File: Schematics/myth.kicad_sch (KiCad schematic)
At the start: 135 parts, among them J1 Conn_01x08_Male, J10 Conn_01x04_Male, J11 Conn_02x01, J2 Conn_01x08_Male, J3 Conn_01x08_Male, J4 Conn_01x08_Male, J5 Conn_01x08_Male, J6 Conn_01x08_Male, J8 Conn_01x08_Male, J9 Conn_01x04_Male, U1 74AHC02, U10 74HC595, U11 74HC165, U12 74AHC08, U13 74HC238, U14 74HC238, U15 74HC238, U16 4002, U17 74HC32, U18 74AHC273, U19 74LS32, U2 74AHC273, U20 CD4532BE, U21 74AHC138, U22 74AHC04, U23 74AHC138, U24 74HC238, U25 74HC238, U26 74LS32, U27 4078, U28 74AHC244, U29 74AHC138, U3 74HC74, U30 74AHC138, U31 4075, U32 74AHC02, U33 74AHC138, U34 74HC238, U35 74AHC138, U36 74HC163, U37 74AHC574, U38 74HC238, U39 74HC32, U4 74AHC04, U40 74AHC04, U41 74AHC574, U42 74HC74, U43 74AHC273, U44 74HC283, U45 74HC283, U46 74AHC273, U47 74HC02, U48 74HC157, U49 74HC157, U5 74AHC04, U50 74AHC244, U51 74AHC04, U52 74AHC574, U53 74HC193, U54 74HC193, U55 74HC193, U56 74HC193, U57 74HC193, U58 74HC193, U59 74HC193, U6 74AHC08, U60 74AHC244, U61 74LS32, U62 4078, U63 74AHC244, U64 74LS21, U65 74AHC04, U66 74AHC273, U67 74HC157, U68 74HC157, U69 74HC157, U7 74HC00, U70 74HC157, U71 74LS257, U72 74LS257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

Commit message: Change GETPUT opcode encoding
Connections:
- net IB0: now also U75.2 (1A0); no longer U9.1 (A0)
- net IB1: now also U75.4 (1A1); no longer U9.2 (A1)
- net IB2: now also U75.6 (1A2); no longer U9.3 (A2)
- net IB3: now also U9.3 (A2); no longer U75.2 (1A0)
- net IB4: now also U9.1 (A0); no longer U75.4 (1A1)
- net IB5: now also U9.2 (A1); no longer U75.6 (1A2)
- net PAR_CP renamed SH1_PARCP
- net ~{PAR_OE} renamed ~{SL1_PAROE}
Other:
- note added: "IB 0-2 are the immediate offset for GET-PUT operations"
- note added: "IB0-2 is byte offset"
- note added: "Instruction byte: all0: OPC_SYS 00000 xxx See table @ SYS decoder else: OPC_ADJUST 00001 xxx b2:extended sign bit b1-0 LSB OPC_ALU 0001x xxx See table @ ALU OPC_TRAP 001xx xxx b4:MSB b3-0:LSB (remaining bits set 1) OPC_GETPUT 01xxx xxx b0-2 OFFS b3:GP B4-5:REG(RODG) OPC_PAIR 1xxxx xxx DEST SRC"
- note added: "NML => INO NMD => DEO MLML => NOP (reserved) MLML => NOP (reserved) MDML => NOP (reserved) MDMD => NOP (reserved) GG => NOP (reserved) RR => NOP (reserved) II => NOP (reserved)"
- note added: "Remap ("scrounge") GG, RR, II etc, and impracticable opcodes such as N-MD"
- note added: "SH0_NULL device"
- note added: "~{SL0_NULL} device"
- note removed: "IB 3-5 are the immediate offset for GET-PUT operations"
- note removed: "IB3-5 is byte offset"
- note removed: "Instruction byte: all0: OPC_SYS 00000 xxx See table @ SYS decoder else: OPC_ADJUST 00001 xxx b2:extended sign bit b1-0 LSB OPC_ALU 0001x xxx See table @ ALU OPC_TRAP 001xx xxx b4:MSB b3-0:LSB (remaining bits set 1) OPC_GETPUT 01xxx xxx b5-3 OFFS b2:GL b1:GP B0:RO OPC_PAIR 1xxxx xxx DEST SRC"
- note removed: "NULL device"
- note removed: "Remap ("scrounge") RR, II etc, and impracticable opcodes such as N-MD"
- moved on the sheet: U18, U24, U25, U29, U30

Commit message: Update schematics file
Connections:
- net MDx renamed Mx
- net MDx_pre renamed Mx_pre
- net MLx renamed Lx
- net MLx_pre renamed Lx_pre
- net xGI renamed xA
- net xJF renamed xF
- net xJT renamed xT
- net xJW renamed xW
- net xJW_pre renamed xW_pre
- net xMD_pre renamed xM_pre
- net xML_pre renamed xL_pre
- net ~{MDx} renamed ~{Mx}
- net ~{MLx} renamed ~{Lx}
- net ~{xJW} renamed ~{xW}
- net ~{xMD} renamed ~{xM}
- net ~{xML} renamed ~{xL}
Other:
- note added: "NL => INO NM => DEO LL => NOP (reserved) LM => NOP (reserved) ML => NOP (reserved) MM => NOP (reserved) GG => NOP (reserved) RR => NOP (reserved) II => NOP (reserved)"
- note added: "Remap ("scrounge") GG, RR, II etc, and impracticable opcodes such as NM"
- note added: "To do: Fix logic above to map NL to INO, and NM to DEO"
- note removed: "NML => INO NMD => DEO MLML => NOP (reserved) MLML => NOP (reserved) MDML => NOP (reserved) MDMD => NOP (reserved) GG => NOP (reserved) RR => NOP (reserved) II => NOP (reserved)"
- note removed: "Remap ("scrounge") GG, RR, II etc, and impracticable opcodes such as N-MD"
- note removed: "To do: Fix logic above to map NML to INO, and NMD to DEO"
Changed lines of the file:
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@@
 		)
 	)
-	(text "                   NML  => INO\n                   NMD  => DEO\n                   MLML => NOP (reserved)\n                   MLML => NOP (reserved)\n                   MDML => NOP (reserved)\n                   MDMD => NOP (reserved)\n                   GG   => NOP (reserved)\n                   RR   => NOP (reserved)\n                   II   => NOP (reserved)"
+	(text "                   NL => INO\n                   NM => DEO\n                   LL => NOP (reserved)\n                   LM => NOP (reserved)\n                   ML => NOP (reserved)\n                   MM => NOP (reserved)\n                   GG => NOP (reserved)\n                   RR => NOP (reserved)\n                   II => NOP (reserved)"
 		(exclude_from_sim no)
 		(at 188.028 312.557 0)
@@
 		)
 	)
-	(text "To do:\nFix logic above\nto map NML to INO,\nand NMD to DEO"
+	(text "To do:\nFix logic above\nto map NL to INO,\nand NM to DEO"
 		(exclude_from_sim no)
 		(at 190.62 300.8412 0)
@@
 		)
 	)
-	(text "Remap (\"scrounge\") GG, RR, II etc,\nand impracticable opcodes such as N-MD"
+	(text "Remap (\"scrounge\") GG, RR, II etc,\nand impracticable opcodes such as NM"
 		(exclude_from_sim no)
 		(at 219.7394 228.2457 0)
@@
 		)
 	)
-	(label "~{MDx}"
+	(label "~{Mx}"
 		(at 705.7307 273.4183 180)
 		(fields_autoplaced yes)
@@
 		)
 	)
-	(label "~{xMD}"
+	(label "~{xM}"
 		(at 1123.5198 503.8164 0)
 		(fields_autoplaced yes)
@@
 		)
 	)
-	(label "xJT"
+	(label "xT"
 		(at 63.9318 196.3674 180)
 		(fields_autoplaced yes)
@@
 		)
 	)
-	(label "xJW"
+	(label "xW"
 		(at 745.0077 134.3281 180)
 		(fields_autoplaced yes)
@@
 		)
 	)
-	(label "xGI"
+	(label "xA"
 		(at 364.9218 304.4698 0)
 		(fields_autoplaced yes)
@@
 		)
 	)
-	(label "xJW_pre"
+	(label "xW_pre"
 		(at 63.9318 191.2874 180)
 		(fields_autoplaced yes)
@@
 		)
 	)
-	(label "~{xML}"
+	(label "~{xL}"
 		(at 364.2868 268.9098 0)
 		(fields_autoplaced yes)
@@
 		)
 	)
-	(label "MDx_pre"
+	(label "Mx_pre"
 		(at 137.3886 380.1872 0)
 		(fields_autoplaced yes)
@@
 		)
 	)
-	(label "MLx"
+	(label "Lx"
 		(at 759.5384 199.9363 0)
 		(fields_autoplaced yes)
@@
 		)
 	)
-	(label "~{xML}"
+	(label "~{xL}"
 		(at 1123.5198 506.3564 0)
 		(fields_autoplaced yes)
@@
 		)
 	)
-	(label "xMD_pre"
+	(label "xM_pre"
 		(at 957.9938 695.1442 180)
 		(fields_autoplaced yes)
@@
 		)
 	)
-	(label "MLx_pre"
+	(label "Lx_pre"
 		(at 137.3886 382.7272 0)
 		(fields_autoplaced yes)
@@
 		)
 	)
-	(label "MDx_pre"
+	(label "Mx_pre"
 		(at 957.9938 690.0642 180)
 		(fields_autoplaced yes)
@@
 		)
 	)
-	(label "xGI"
+	(label "xA"
 		(at 594.1685 186.1343 180)
 		(fields_autoplaced yes)
@@
 		)
 	)
-	(label "~{xJW}"
+	(label "~{xW}"
 		(at 760.2477 134.3281 0)
 		(fields_autoplaced yes)
@@
 		)
 	)
-	(label "MLx_pre"
+	(label "Lx_pre"
 		(at 703.1814 523.1929 180)
 		(fields_autoplaced yes)
@@
 		)
 	)
-	(label "xGI"
+	(label "xA"
 		(at 562.7742 167.7322 180)
 		(fields_autoplaced yes)
@@
 		)
 	)
-	(label "xJW_pre"
+	(label "xW_pre"
 		(at 131.6482 269.5702 0)
 		(fields_autoplaced yes)
@@
 		)
 	)
-	(label "xJT"
+	(label "xT"
 		(at 364.9218 314.6298 0)
 		(fields_autoplaced yes)
@@
 		)
 	)
-	(label "MDx"
+	(label "Mx"
 		(at 720.9707 273.4183 0)
 		(fields_autoplaced yes)
@@
 		)
 	)
-	(label "xML_pre"
+	(label "xL_pre"
 		(at 175.1584 279.1714 180)
 		(fields_autoplaced yes)
@@
 		)
 	)
-	(label "~{MDx}"
+	(label "~{Mx}"
 		(at 362.3818 376.2248 0)
 		(fields_autoplaced yes)
@@
 		)
 	)
-	(label "xJF"
+	(label "xF"
 		(at 364.9218 317.1698 0)
 		(fields_autoplaced yes)
@@
 		)
 	)
-	(label "~{xMD}"
+	(label "~{xM}"
 		(at 364.2868 266.3698 0)
 		(fields_autoplaced yes)
@@
 		)
 	)
-	(label "xML_pre"
+	(label "xL_pre"
 		(at 131.1148 316.5348 0)
 		(fields_autoplaced yes)
@@
 		)
 	)
-	(label "~{MLx}"
+	(label "~{Lx}"
 		(at 744.2984 199.9363 180)
 		(fields_autoplaced yes)
@@
 		)
 	)
-	(label "MLx"
+	(label "Lx"
 		(at 1109.2883 604.7814 0)
 		(fields_autoplaced yes)
@@
 		)
 	)
-	(label "xMD_pre"
+	(label "xM_pre"
 		(at 131.1148 313.9948 0)
 		(fields_autoplaced yes)
@@
 		)
 	)
-	(label "MDx_pre"
+	(label "Mx_pre"
 		(at 174.9866 261.5757 180)
 		(fields_autoplaced yes)
@@
 		)
 	)
-	(label "MDx"
+	(label "Mx"
 		(at 1109.2883 602.2414 0)
 		(fields_autoplaced yes)
@@
 		)
 	)
-	(label "~{xJW}"
+	(label "~{xW}"
 		(at 631.5591 667.5672 180)
 		(fields_autoplaced yes)
@@
 		)
 	)
-	(label "xMD_pre"
+	(label "xM_pre"
 		(at 175.1584 284.2514 180)
 		(fields_autoplaced yes)
@@
 		)
 	)
-	(label "xGI"
+	(label "xA"
 		(at 562.9238 225.3634 180)
 		(fields_autoplaced yes)
@@
 		)
 	)
-	(label "xJW"
+	(label "xW"
 		(at 364.9218 312.0898 0)
 		(fields_autoplaced yes)
@@
 		)
 	)
-	(label "xJF"
+	(label "xF"
 		(at 63.9318 198.9074 180)
 		(fields_autoplaced yes)
@@
 		)
 	)
-	(label "MLx_pre"
+	(label "Lx_pre"
 		(at 174.9866 256.4957 180)
 		(fields_autoplaced yes)
@@
 		)
 	)
-	(label "~{MLx}"
+	(label "~{Lx}"
 		(at 362.3818 378.7648 0)
 		(fields_autoplaced yes)
@@
 		)
 	)
-	(label "xML_pre"
+	(label "xL_pre"
 		(at 703.1814 528.2729 180)
 		(fields_autoplaced yes)

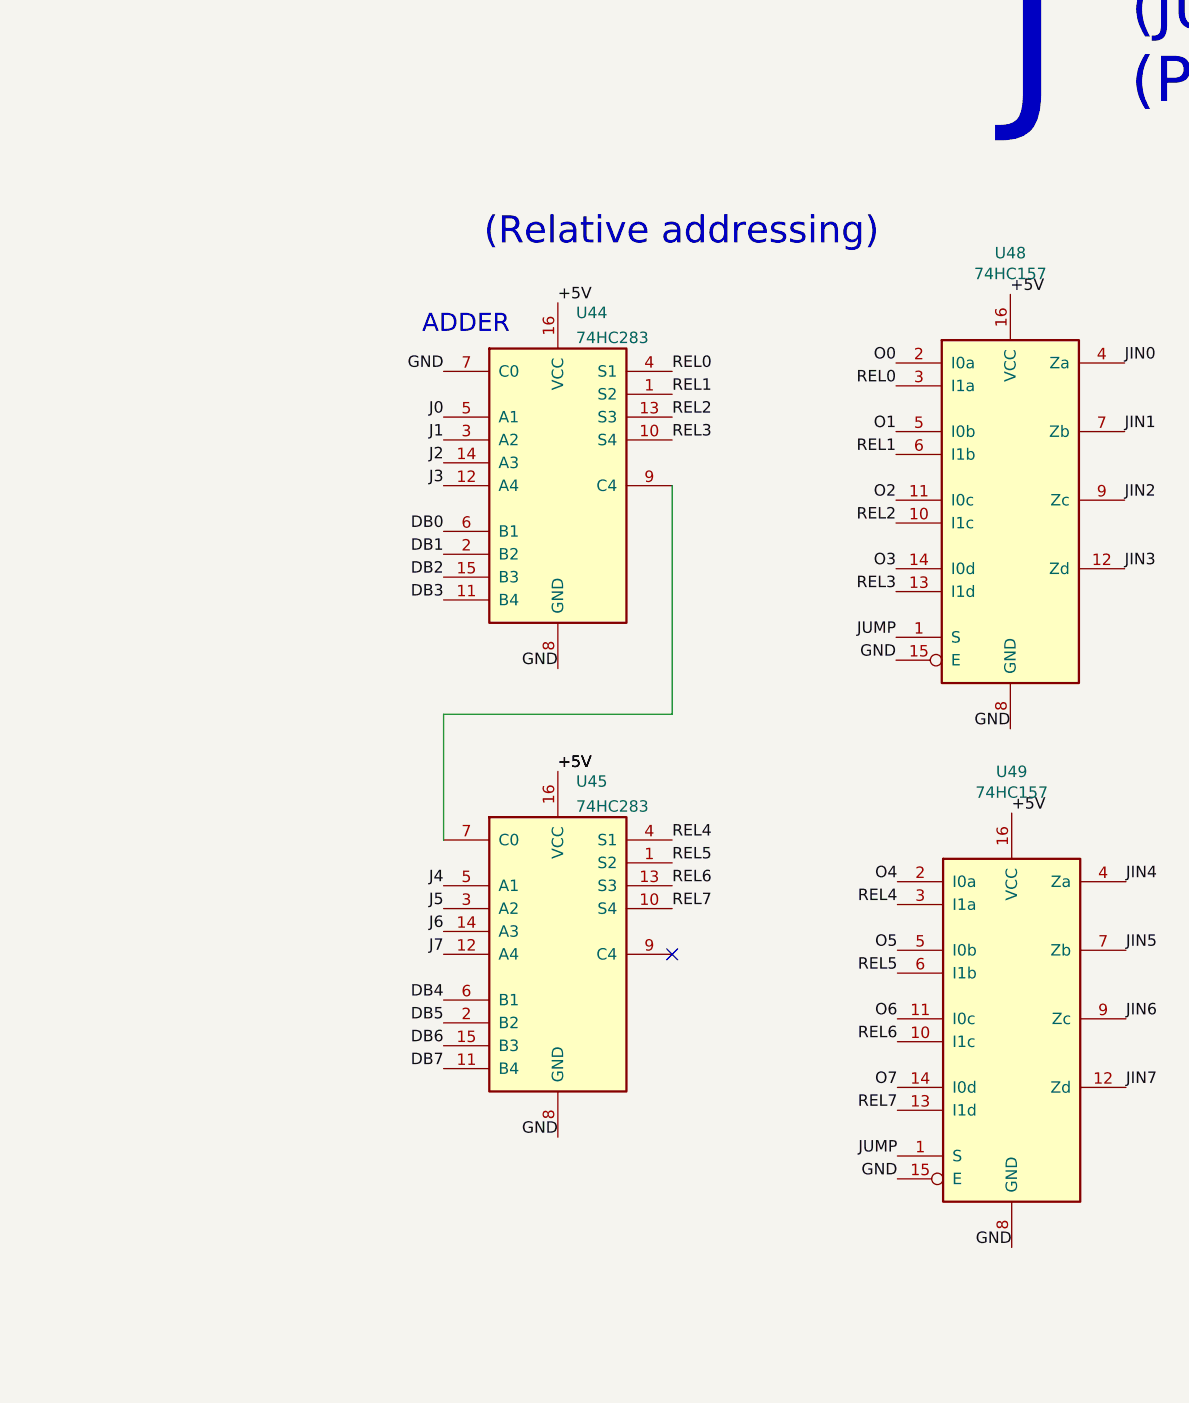
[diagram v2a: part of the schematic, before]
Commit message: Switch back to absolute addressing
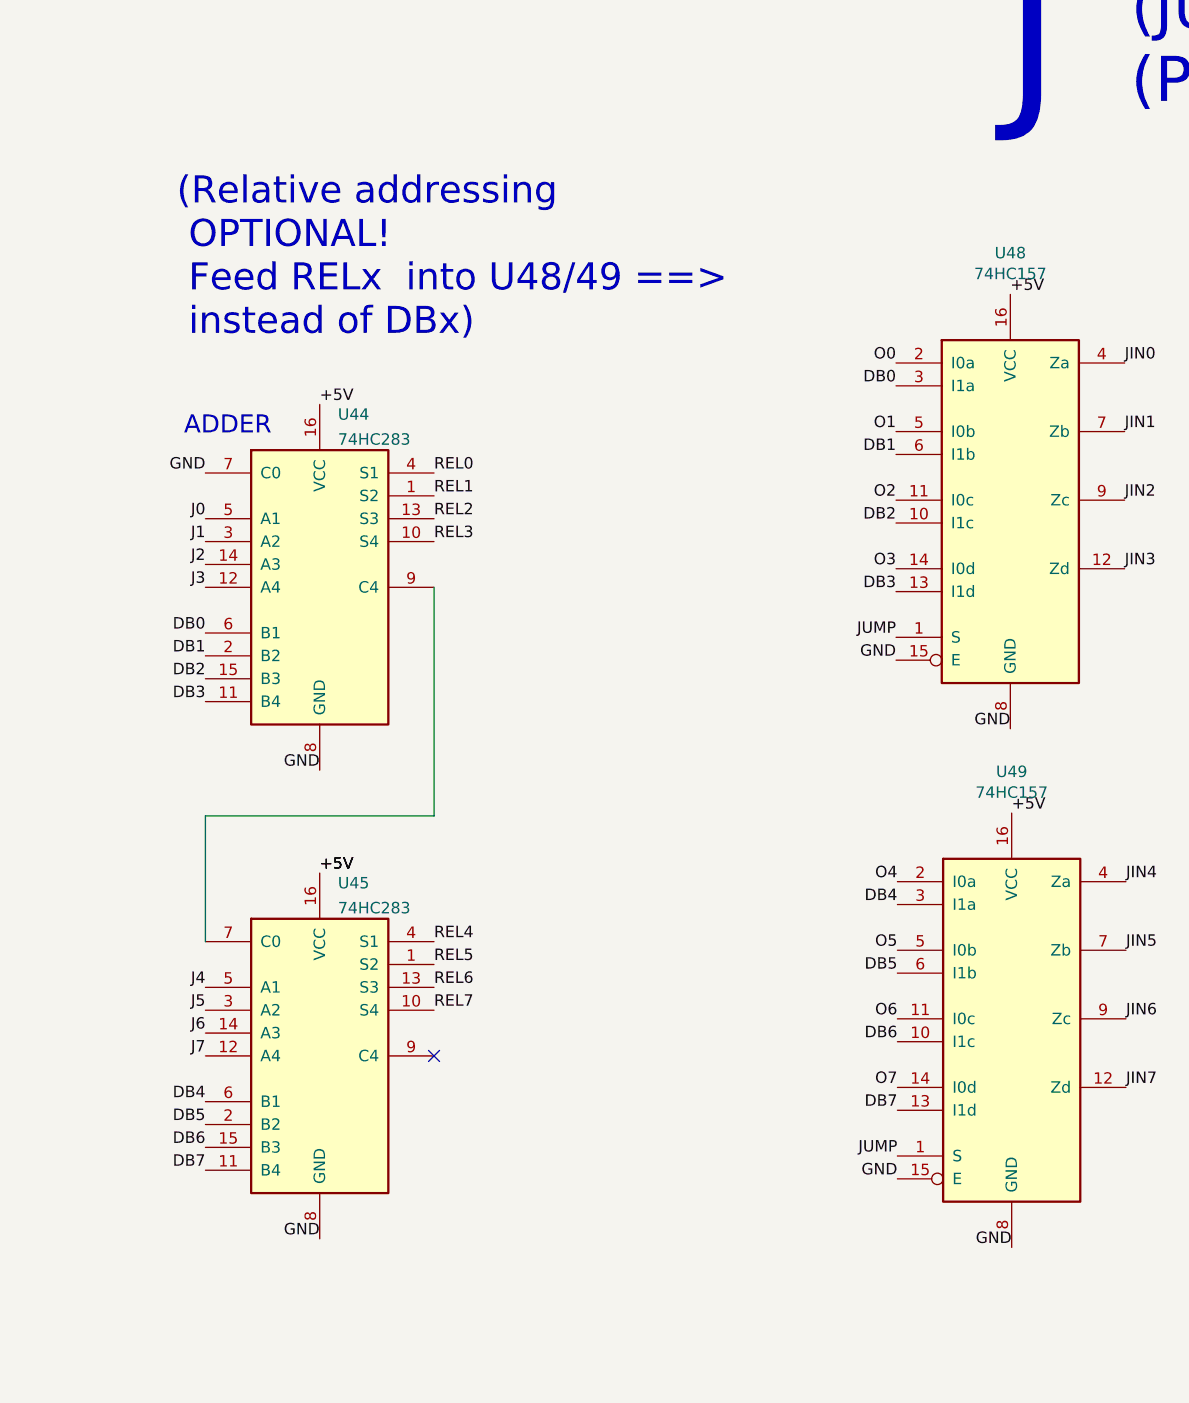
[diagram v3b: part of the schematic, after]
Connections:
- net DB0: now also U48.3 (I1a)
- net DB1: now also U48.6 (I1b)
- net DB2: now also U48.10 (I1c)
- net DB3: now also U48.13 (I1d)
- net DB4: now also U49.3 (I1a)
- net DB5: now also U49.6 (I1b)
- net DB6: now also U49.10 (I1c)
- net DB7: now also U49.13 (I1d)
- net REL0: no longer U48.3 (I1a)
- net REL1: no longer U48.6 (I1b)
- net REL2: no longer U48.10 (I1c)
- net REL3: no longer U48.13 (I1d)
- net REL4: no longer U49.3 (I1a)
- net REL5: no longer U49.6 (I1b)
- net REL6: no longer U49.10 (I1c)
- net REL7: no longer U49.13 (I1d)
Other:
- note added: "(Relative addressing OPTIONAL! Feed RELx into U48/49 ==> instead of DBx)"
- note removed: "(Relative addressing)"
- moved on the sheet: U44, U45
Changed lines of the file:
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@@
 	(title_block
 		(title "Sonne-8 Micro-Controller")
-		(date "2024-08-25")
+		(date "2024-08-26")
 		(rev "Myth")
 		(company "Contact: mim@ok-schalter.de")
@@
 	)
 	(no_connect
-		(at 472.4824 406.8887)
+		(at 446.0236 418.1813)
 	)
 	(no_connect
@@
 	(wire
 		(pts
-			(xy 447.0824 380.2187) (xy 447.0824 394.1887)
+			(xy 420.6236 391.5113) (xy 420.6236 405.4813)
 		)
 		(stroke
@@
 	(wire
 		(pts
-			(xy 472.4824 354.8187) (xy 472.4824 380.2187)
+			(xy 446.0236 366.1113) (xy 446.0236 391.5113)
 		)
 		(stroke
@@
 	(wire
 		(pts
-			(xy 472.4824 380.2187) (xy 447.0824 380.2187)
+			(xy 446.0236 391.5113) (xy 420.6236 391.5113)
 		)
 		(stroke
@@
 		)
 	)
-	(text "(Relative addressing)"
+	(text "(Relative addressing\n OPTIONAL!\n Feed RELx  into U48/49 ==>\n instead of DBx)\n"
 		(exclude_from_sim no)
-		(at 451.5615 328.3983 0)
+		(at 417.4367 338.4544 0)
 		(effects
 			(font
@@
 	(text "ADDER"
 		(exclude_from_sim no)
-		(at 444.6948 338.1055 0)
+		(at 418.236 349.3981 0)
 		(effects
 			(font
@@
 		)
 	)
-	(label "REL0"
+	(label "DB0"
 		(at 497.3579 343.7277 180)
 		(fields_autoplaced yes)
@@
 	)
 	(label "DB4"
-		(at 447.0824 411.9687 180)
+		(at 420.6236 423.2613 180)
 		(fields_autoplaced yes)
 		(effects
@@
 	)
 	(label "REL6"
-		(at 472.4824 399.2687 0)
+		(at 446.0236 410.5613 0)
 		(fields_autoplaced yes)
 		(effects
@@
 		)
 	)
-	(label "REL2"
+	(label "DB2"
 		(at 497.3579 358.9677 180)
 		(fields_autoplaced yes)
@@
 	)
 	(label "REL1"
-		(at 472.4824 344.6587 0)
+		(at 446.0236 355.9513 0)
 		(fields_autoplaced yes)
 		(effects
@@
 	)
 	(label "DB0"
-		(at 447.0824 359.8987 180)
+		(at 420.6236 371.1913 180)
 		(fields_autoplaced yes)
 		(effects
@@
 	)
 	(label "DB5"
-		(at 447.0824 414.5087 180)
+		(at 420.6236 425.8013 180)
 		(fields_autoplaced yes)
 		(effects
@@
 	)
 	(label "REL7"
-		(at 472.4824 401.8087 0)
+		(at 446.0236 413.1013 0)
 		(fields_autoplaced yes)
 		(effects
@@
 	)
 	(label "GND"
-		(at 447.0824 342.1187 180)
+		(at 420.6236 353.4113 180)
 		(fields_autoplaced yes)
 		(effects
@@
 	)
 	(label "J1"
-		(at 447.0824 349.7387 180)
+		(at 420.6236 361.0313 180)
 		(fields_autoplaced yes)
 		(effects
@@
 	)
 	(label "GND"
-		(at 459.7824 427.2087 180)
+		(at 433.3236 438.5013 180)
 		(fields_autoplaced yes)
 		(effects
@@
 	)
 	(label "J0"
-		(at 447.0824 347.1987 180)
+		(at 420.6236 358.4913 180)
 		(fields_autoplaced yes)
 		(effects
@@
 	)
 	(label "DB3"
-		(at 447.0824 367.5187 180)
+		(at 420.6236 378.8113 180)
 		(fields_autoplaced yes)
 		(effects
@@
 	)
 	(label "+5V"
-		(at 459.7824 334.4987 0)
+		(at 433.3236 345.7913 0)
 		(fields_autoplaced yes)
 		(effects
@@
 	)
 	(label "J2"
-		(at 447.0824 352.2787 180)
+		(at 420.6236 363.5713 180)
 		(fields_autoplaced yes)
 		(effects
@@
 		)
 	)
-	(label "REL4"
+	(label "DB4"
 		(at 497.5075 401.3589 180)
 		(fields_autoplaced yes)
@@
 	)
 	(label "DB2"
-		(at 447.0824 364.9787 180)
+		(at 420.6236 376.2713 180)
 		(fields_autoplaced yes)
 		(effects
@@
 	)
 	(label "DB1"
-		(at 447.0824 362.4387 180)
+		(at 420.6236 373.7313 180)
 		(fields_autoplaced yes)
 		(effects
@@
 	)
 	(label "J5"
-		(at 447.0824 401.8087 180)
+		(at 420.6236 413.1013 180)
 		(fields_autoplaced yes)
 		(effects
@@
 	)
 	(label "J7"
-		(at 447.0824 406.8887 180)
+		(at 420.6236 418.1813 180)
 		(fields_autoplaced yes)
 		(effects
@@
 		)
 	)
-	(label "REL3"
+	(label "DB3"
 		(at 497.3579 366.5877 180)
 		(fields_autoplaced yes)
@@
 	)
 	(label "REL3"
-		(at 472.4824 349.7387 0)
+		(at 446.0236 361.0313 0)
 		(fields_autoplaced yes)
 		(effects
@@
 	)
 	(label "REL0"
-		(at 472.4824 342.1187 0)
+		(at 446.0236 353.4113 0)
 		(fields_autoplaced yes)
 		(effects
@@
 	)
 	(label "J3"
-		(at 447.0824 354.8187 180)
+		(at 420.6236 366.1113 180)
 		(fields_autoplaced yes)
 		(effects
@@
 	)
 	(label "J4"
-		(at 447.0824 399.2687 180)
+		(at 420.6236 410.5613 180)
 		(fields_autoplaced yes)
 		(effects
@@
 	)
 	(label "REL4"
-		(at 472.4824 394.1887 0)
+		(at 446.0236 405.4813 0)
 		(fields_autoplaced yes)
 		(effects
@@
 	)
 	(label "+5V"
-		(at 459.7824 386.5687 0)
+		(at 433.3236 397.8613 0)
 		(fields_autoplaced yes)
 		(effects
@@
 		)
 	)
-	(label "REL1"
+	(label "DB1"
 		(at 497.3579 351.3477 180)
 		(fields_autoplaced yes)
@@
 	)
 	(label "DB7"
-		(at 447.0824 419.5887 180)
+		(at 420.6236 430.8813 180)
 		(fields_autoplaced yes)
 		(effects
@@
 	)
 	(label "REL5"
-		(at 472.4824 396.7287 0)
+		(at 446.0236 408.0213 0)
 		(fields_autoplaced yes)
 		(effects
@@
 		)
 	)
-	(label "REL5"
+	(label "DB5"
 		(at 497.5075 408.9789 180)
 		(fields_autoplaced yes)
@@
 	)
 	(label "REL2"
-		(at 472.4824 347.1987 0)
+		(at 446.0236 358.4913 0)
 		(fields_autoplaced yes)
 		(effects
@@
 	)
 	(label "GND"
-		(at 459.7824 375.1387 180)
+		(at 433.3236 386.4313 180)
 		(fields_autoplaced yes)
 		(effects
@@
 		)
 	)
-	(label "REL6"
+	(label "DB6"
 		(at 497.5075 416.5989 180)
 		(fields_autoplaced yes)
@@
 	)
 	(label "DB6"
-		(at 447.0824 417.0487 180)
+		(at 420.6236 428.3413 180)
 		(fields_autoplaced yes)
 		(effects
@@
 		)
 	)
-	(label "REL7"
+	(label "DB7"
 		(at 497.5075 424.2189 180)
 		(fields_autoplaced yes)
@@
 	)
 	(label "+5V"
-		(at 459.7824 386.5687 0)
+		(at 433.3236 397.8613 0)
 		(fields_autoplaced yes)
 		(effects
@@
 	)
 	(label "J6"
-		(at 447.0824 404.3487 180)
+		(at 420.6236 415.6413 180)
 		(fields_autoplaced yes)
 		(effects
@@
 	(symbol
 		(lib_id "74xx:74LS283")
-		(at 459.7824 354.8187 0)
+		(at 433.3236 366.1113 0)
 		(unit 1)
 		(exclude_from_sim no)
@@
 		(fields_autoplaced yes)
 		(property "Reference" "U44"
-			(at 461.8018 335.6122 0)
+			(at 435.343 346.9048 0)
 			(effects
 				(font
@@
 		)
 		(property "Value" "74HC283"
-			(at 461.8018 338.3873 0)
+			(at 435.343 349.6799 0)
 			(effects
 				(font
@@
 		)
 		(property "Footprint" "Package_DIP:DIP-16_W7.62mm_Socket_LongPads"
-			(at 459.7824 354.8187 0)
+			(at 433.3236 366.1113 0)
 			(effects
 				(font
@@
 		)
 		(property "Datasheet" "http://www.ti.com/lit/gpn/sn74LS283"
-			(at 459.7824 354.8187 0)
+			(at 433.3236 366.1113 0)
 			(effects
 				(font
@@
 		)
 		(property "Description" ""
-			(at 459.7824 354.8187 0)
+			(at 433.3236 366.1113 0)
 			(effects
 				(font
@@
 	(symbol
 		(lib_id "74xx:74LS283")
-		(at 459.7824 406.8887 0)
+		(at 433.3236 418.1813 0)
 		(unit 1)
 		(exclude_from_sim no)
@@
 		(fields_autoplaced yes)
 		(property "Reference" "U45"
-			(at 461.8018 387.6822 0)
+			(at 435.343 398.9748 0)
 			(effects
 				(font
@@
 		)
 		(property "Value" "74HC283"
-			(at 461.8018 390.4573 0)
+			(at 435.343 401.7499 0)
 			(effects
 				(font
@@
 		)
 		(property "Footprint" "Package_DIP:DIP-16_W7.62mm_Socket_LongPads"
-			(at 459.7824 406.8887 0)
+			(at 433.3236 418.1813 0)
 			(effects
 				(font
@@
 		)
 		(property "Datasheet" "http://www.ti.com/lit/gpn/sn74LS283"
-			(at 459.7824 406.8887 0)
+			(at 433.3236 418.1813 0)
 			(effects
 				(font
@@
 		)
 		(property "Description" ""
-			(at 459.7824 406.8887 0)
+			(at 433.3236 418.1813 0)
 			(effects
 				(font
